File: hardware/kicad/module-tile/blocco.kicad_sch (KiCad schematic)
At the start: 52 parts, among them SW1 SW_Push_45deg, SW10 SW_Push_45deg, SW11 SW_Push_45deg, SW12 SW_Push_45deg, SW2 SW_Push_45deg, SW3 SW_Push_45deg, SW4 SW_Push_45deg, SW5 SW_Push_45deg, SW6 SW_Push_45deg, SW7 SW_Push_45deg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

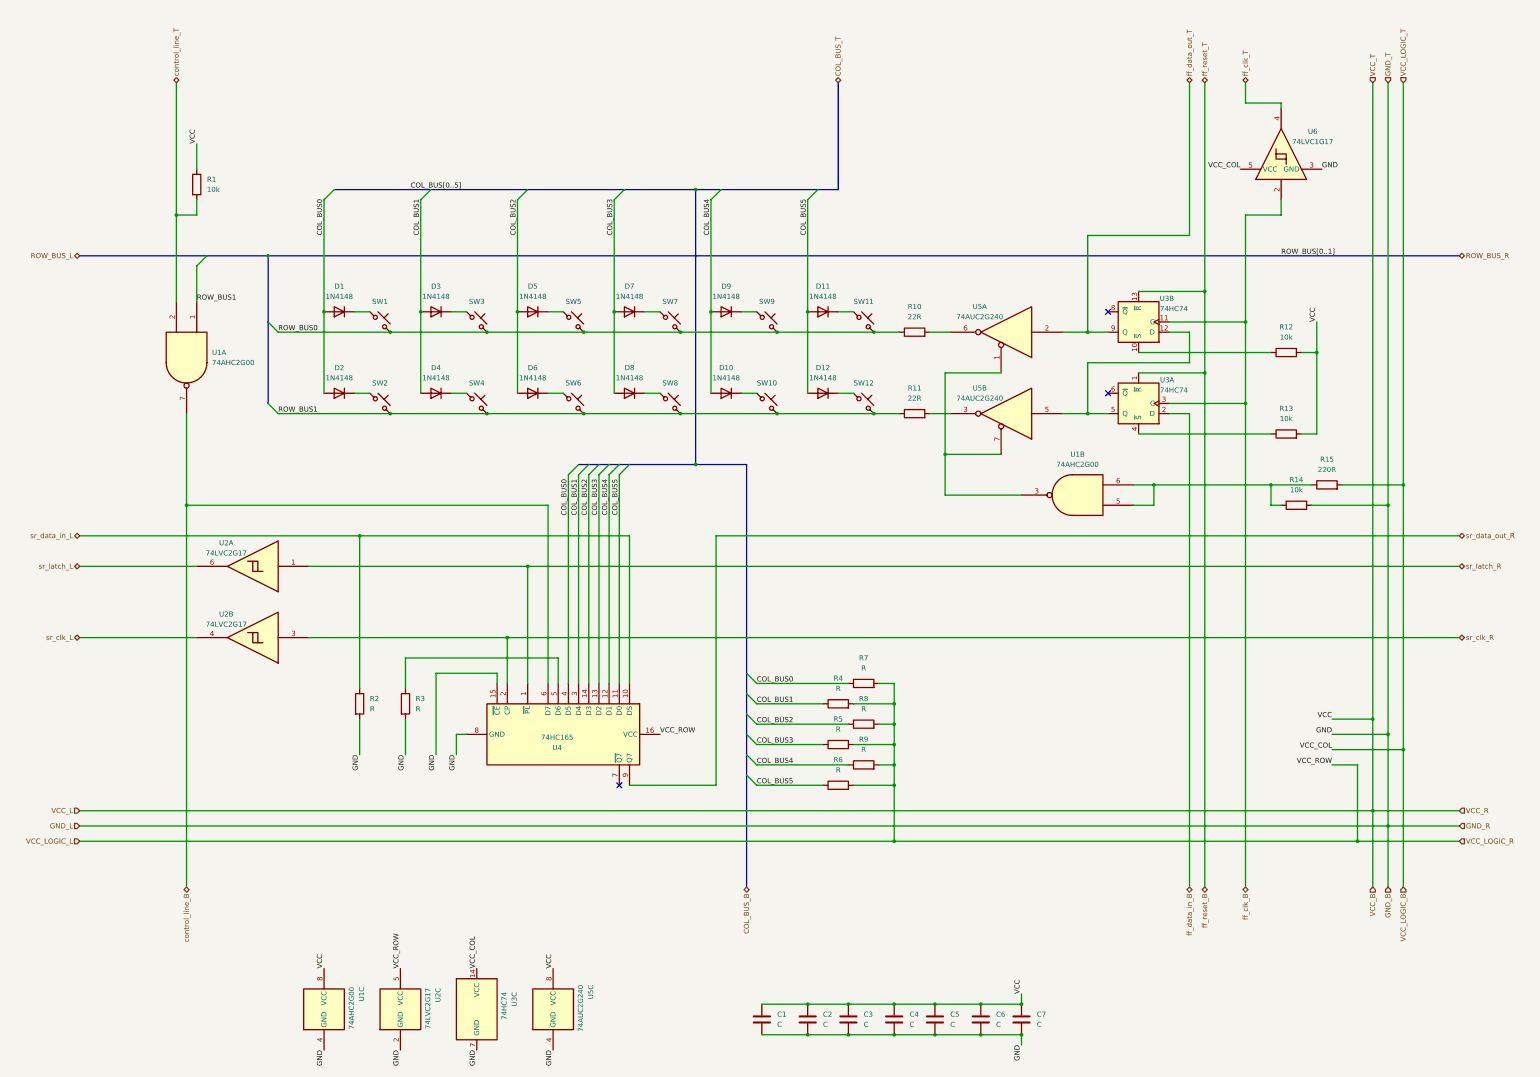
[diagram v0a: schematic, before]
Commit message: Added horizontal control line UTF-8 like. Updated capacitor and resistor values.
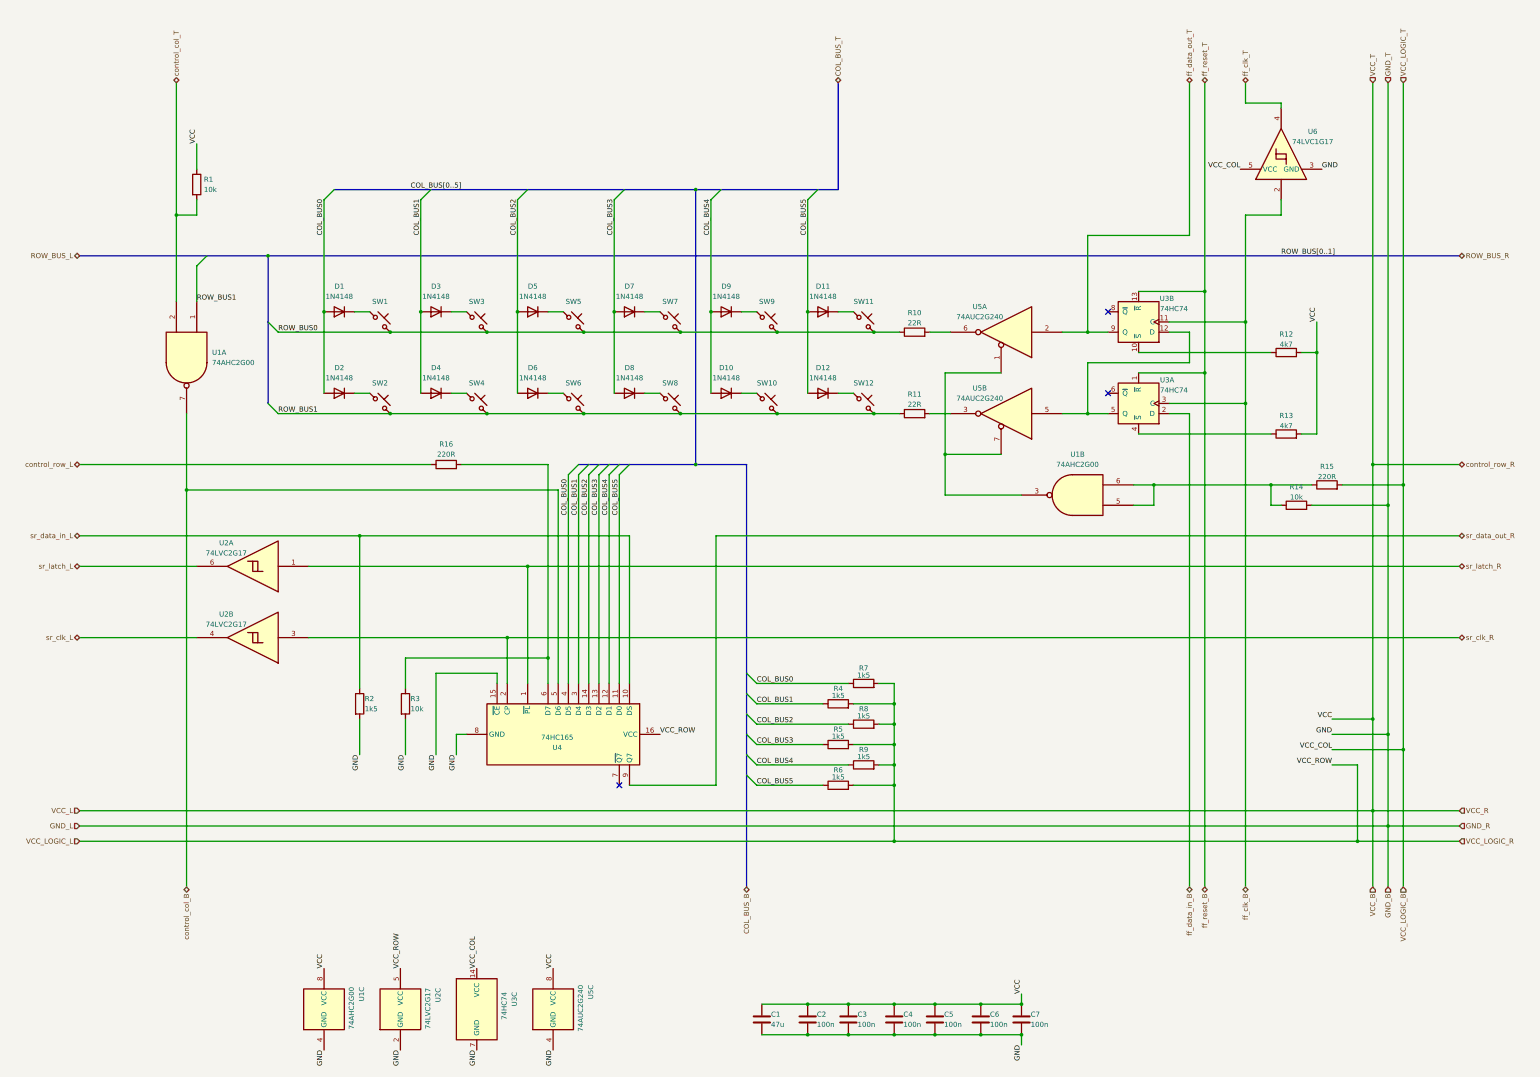
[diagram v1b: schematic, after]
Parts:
- added R16: 220R, symbol Device:R
- C1: value C -> 47u
- C2, C3, C4, C5, C6, C7: value C -> 100n
- R12, R13: value 10k -> 4k7
- R2, R4, R5, R6, R7, R8, R9: value R -> 1k5
- R3: value R -> 10k
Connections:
- net at R3.1: now also U4.6 (D7), R16.2; no longer U4.5 (D6)
- net control_line_B renamed control_col_B
- net control_col_B: now also U4.5 (D6); no longer U4.6 (D7)
- net control_line_T renamed control_col_T
- new net control_row_L: R16.1
